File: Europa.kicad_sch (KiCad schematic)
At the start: 0 parts

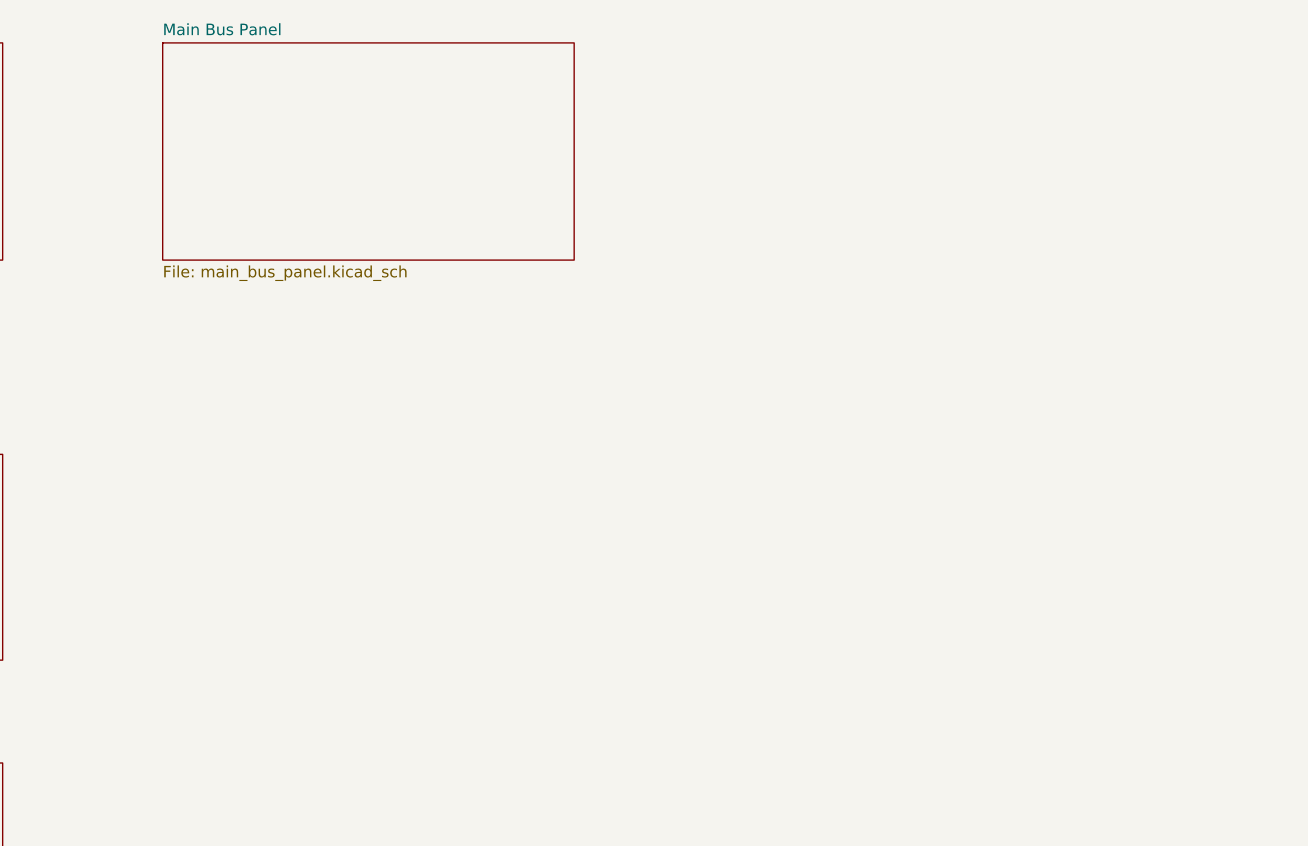
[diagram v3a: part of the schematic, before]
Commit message: Added Trim Circuit and Avionics Bus
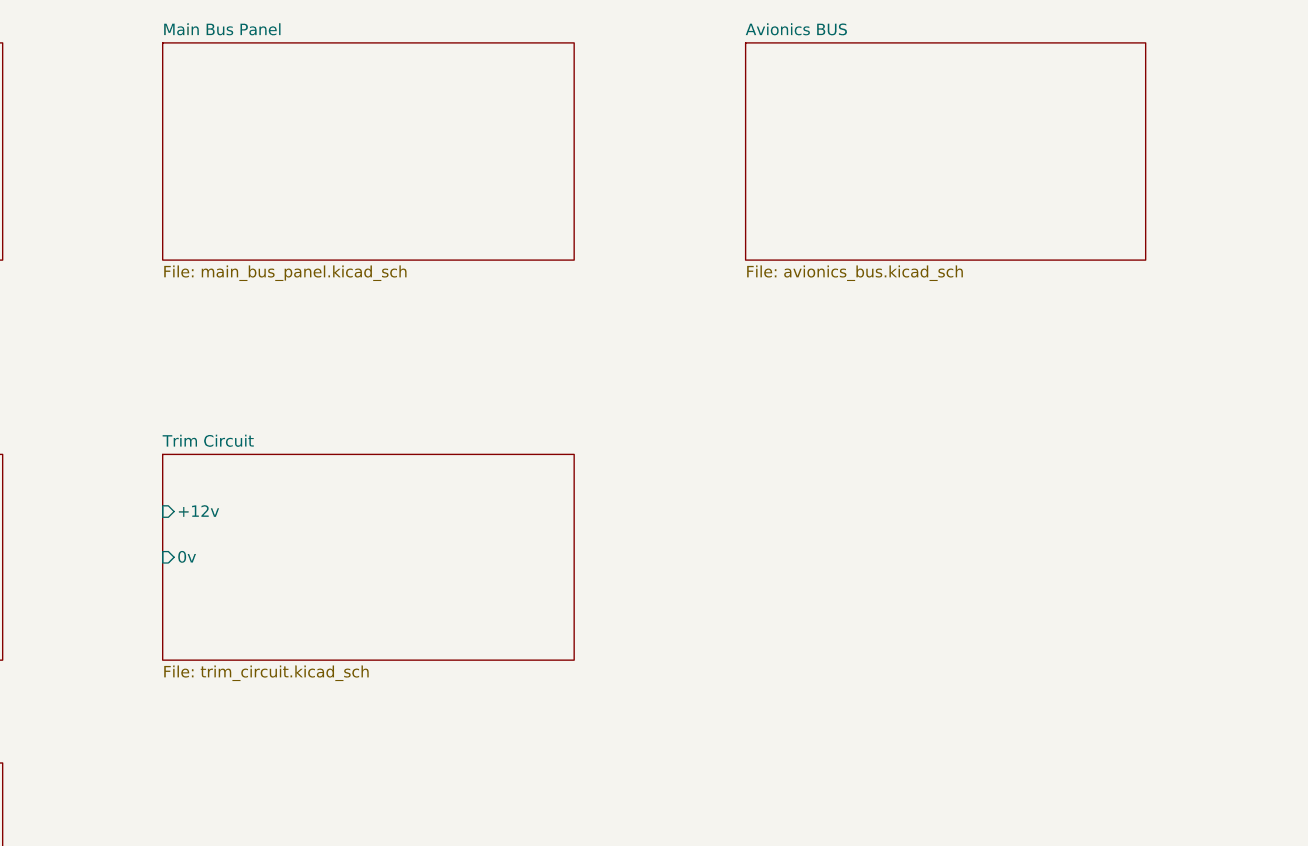
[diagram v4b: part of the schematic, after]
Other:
- added sheet Avionics BUS (avionics_bus.kicad_sch)
- added sheet Trim Circuit (trim_circuit.kicad_sch)
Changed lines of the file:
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@@
+    )
+  )
+  (sheet (at 157.48 29.21) (size 44.45 24.13) (fields_autoplaced)
+    (stroke (width 0.1524) (type solid) (color 0 0 0 0))
+    (fill (color 0 0 0 0.0000))
+    (property "Sheet name" "Avionics BUS" (id 0) (at 157.48 28.4984 0)
+      (effects (font (size 1.27 1.27)) (justify left bottom))
+    )
+    (property "Sheet file" "avionics_bus.kicad_sch" (id 1) (at 157.48 53.9246 0)
+      (effects (font (size 1.27 1.27)) (justify left top))
     )
   )
@@
     (property "Sheet file" "com.kicad_sch" (id 1) (at 232.41 114.8846 0)
       (effects (font (size 1.27 1.27)) (justify left top))
+    )
+  )
+  (sheet (at 92.71 74.93) (size 45.72 22.86) (fields_autoplaced)
+    (stroke (width 0.1524) (type solid) (color 0 0 0 0))
+    (fill (color 0 0 0 0.0000))
+    (property "Sheet name" "Trim Circuit" (id 0) (at 92.71 74.2184 0)
+      (effects (font (size 1.27 1.27)) (justify left bottom))
+    )
+    (property "Sheet file" "trim_circuit.kicad_sch" (id 1) (at 92.71 98.3746 0)
+      (effects (font (size 1.27 1.27)) (justify left top))
+    )
+    (pin "+12v" input (at 92.71 81.28 180)
+      (effects (font (size 1.27 1.27)) (justify left))
+    )
+    (pin "0v" input (at 92.71 86.36 180)
+      (effects (font (size 1.27 1.27)) (justify left))
     )
   )
@@
     (path "/c5676131-d5a4-4fde-914f-3f396c9cd255" (page "6"))
     (path "/e876c59e-4288-4b76-b538-81605be93f21" (page "7"))
+    (path "/866b3cfa-81f9-4c05-8259-46d4a400c4a9" (page "8"))
+    (path "/5afc04a8-14bc-4c25-8a7e-c4e01fd6c06c" (page "9"))
   )
   (symbol_instances
@@
       (reference "#PWR?") (unit 1) (value "GND") (footprint "")
     )
+    (path "/866b3cfa-81f9-4c05-8259-46d4a400c4a9/d0c3bae4-0af2-4e00-b106-8d7e92467906"
+      (reference "#PWR?") (unit 1) (value "GND") (footprint "")
+    )
     (path "/95e96eec-8054-412c-b439-e274da9864da/d8bf2695-17a9-416c-aba7-6777ceba8849"
+      (reference "#PWR?") (unit 1) (value "GND") (footprint "")
+    )
+    (path "/e876c59e-4288-4b76-b538-81605be93f21/e3dea152-b7e9-4b86-892e-d6d245a5440c"
+      (reference "#PWR?") (unit 1) (value "GND") (footprint "")
+    )
+    (path "/866b3cfa-81f9-4c05-8259-46d4a400c4a9/f5636c71-23a5-4c88-8117-e2a6e826ce57"
       (reference "#PWR?") (unit 1) (value "GND") (footprint "")
     )
@@
       (reference "CB?") (unit 1) (value "RDAC CB") (footprint "")
     )
+    (path "/5afc04a8-14bc-4c25-8a7e-c4e01fd6c06c/369404a4-9680-4315-bc28-57fc9db44996"
+      (reference "CB?") (unit 1) (value "Avionics Bus CB") (footprint "")
+    )
     (path "/e876c59e-4288-4b76-b538-81605be93f21/388762f5-890b-46d3-9653-5b33ed052fa1"
       (reference "CB?") (unit 1) (value "Battery Master CB") (footprint "")
@@
       (reference "CB?") (unit 1) (value "Lamps CB") (footprint "")
     )
+    (path "/866b3cfa-81f9-4c05-8259-46d4a400c4a9/8c04583f-084d-417b-adcb-af5504f6662f"
+      (reference "CB?") (unit 1) (value "CircuitBreaker_1P") (footprint "")
+    )
     (path "/e876c59e-4288-4b76-b538-81605be93f21/91d337f0-0505-4fcb-92a1-e365f6ea2f61"
       (reference "CB?") (unit 1) (value "TRIM CB") (footprint "")
@@
       (reference "J4") (unit 1) (value "Screw_Terminal_01x12") (footprint "")
     )
+    (path "/866b3cfa-81f9-4c05-8259-46d4a400c4a9/1fb7f398-44df-4201-bc2f-b642988d115e"
+      (reference "J?") (unit 1) (value "PL?") (footprint "")
+    )
     (path "/c5676131-d5a4-4fde-914f-3f396c9cd255/2b931534-dcf4-4f0a-91cc-dc769096fa05"
       (reference "J?") (unit 1) (value "DB9_Female") (footprint "")
@@
       (reference "J?") (unit 1) (value "DB15_Male") (footprint "")
     )
+    (path "/866b3cfa-81f9-4c05-8259-46d4a400c4a9/3fd3a499-d077-4b88-94d8-a82d86dba2b8"
+      (reference "J?") (unit 1) (value "PL?") (footprint "")
+    )
     (path "/e876c59e-4288-4b76-b538-81605be93f21/619ed128-9b69-4240-9409-37a06185dd84"
       (reference "J?") (unit 1) (value "PL? - Fuel Pump") (footprint "")
@@
       (reference "J?") (unit 1) (value "DB25_Female") (footprint "")
     )
+    (path "/866b3cfa-81f9-4c05-8259-46d4a400c4a9/9c4ce566-e3f9-4617-a008-e8f5eae99ff8"
+      (reference "J?") (unit 1) (value "PL15/3") (footprint "")
+    )
     (path "/c5676131-d5a4-4fde-914f-3f396c9cd255/9d2c5c72-5033-4e18-8ccb-6942d4705a16"
       (reference "J?") (unit 1) (value "DB15_Female") (footprint "")
@@
       (reference "J?") (unit 1) (value "DB15_Male") (footprint "")
     )
+    (path "/5afc04a8-14bc-4c25-8a7e-c4e01fd6c06c/b68e1cf4-a1ec-46c0-9ae1-d5bf2316ba50"
+      (reference "J?") (unit 1) (value "ECB Outputs") (footprint "")
+    )
     (path "/c5676131-d5a4-4fde-914f-3f396c9cd255/c04e6087-e529-408a-8a03-5605e6e4e80a"
       (reference "J?") (unit 1) (value "DB15_Female") (footprint "")
@@
       (reference "J?") (unit 1) (value "DB9_Male") (footprint "")
     )
+    (path "/866b3cfa-81f9-4c05-8259-46d4a400c4a9/cc93d801-b764-4613-8402-e8ad74cecd74"
+      (reference "J?") (unit 1) (value "PL?") (footprint "")
+    )
     (path "/c5676131-d5a4-4fde-914f-3f396c9cd255/d008d60e-b61b-4155-beb9-5029ffe66249"
       (reference "J?") (unit 1) (value "DB9_Male") (footprint "")
     )
+    (path "/866b3cfa-81f9-4c05-8259-46d4a400c4a9/d80e3ef4-71ab-401a-85af-2c0cbb43f9c9"
+      (reference "J?") (unit 1) (value "PL?") (footprint "")
+    )
+    (path "/5afc04a8-14bc-4c25-8a7e-c4e01fd6c06c/dd7940dc-a753-4039-9d10-ba42224e15f4"
+      (reference "J?") (unit 1) (value "DB9_Female") (footprint "")
+    )
     (path "/a5352cd5-5c6a-411a-b1fe-0b8c42ec40dc/e77952fd-3f26-43bd-9da9-266d1d56298c"
       (reference "J?") (unit 1) (value "DB9_Female") (footprint "")
     )
+    (path "/5afc04a8-14bc-4c25-8a7e-c4e01fd6c06c/f42ae037-2e0e-42dc-a666-25d17c484087"
+      (reference "J?") (unit 1) (value "Screw_Terminal_01x01") (footprint "")
+    )
+    (path "/5afc04a8-14bc-4c25-8a7e-c4e01fd6c06c/f8ad658e-16f3-423c-8f3d-ad5f4ce096af"
+      (reference "J?") (unit 1) (value "DB9_Male") (footprint "")
+    )
+    (path "/5afc04a8-14bc-4c25-8a7e-c4e01fd6c06c/fa3f87b1-63e0-4bcf-bfa3-d9d58049cb4a"
+      (reference "J?") (unit 1) (value "Conn_02x08_Odd_Even") (footprint "")
+    )
+    (path "/5afc04a8-14bc-4c25-8a7e-c4e01fd6c06c/fc3384d7-5dd0-4e7d-a6cd-f7d07b72acd5"
+      (reference "J?") (unit 1) (value "Conn_02x08_Odd_Even") (footprint "")
+    )
     (path "/95e96eec-8054-412c-b439-e274da9864da/381197e2-b232-4b8f-b646-39112473a836"
       (reference "LA?") (unit 1) (value "Alternator Warning Lamp") (footprint "")
     )
-    (path "/e876c59e-4288-4b76-b538-81605be93f21/5bf7dce5-2000-421b-958d-68d2519ed3ba"
-      (reference "LA?") (unit 1) (value "Lamp") (footprint "")
-    )
-    (path "/e876c59e-4288-4b76-b538-81605be93f21/b6037f4d-1b39-4027-b890-d8a4414367a5"
-      (reference "LA?") (unit 1) (value "Lamp") (footprint "")
-    )
-    (path "/e876c59e-4288-4b76-b538-81605be93f21/da0418c1-ec5c-46e4-a289-eb3cf882a2aa"
-      (reference "LA?") (unit 1) (value "Lamp") (footprint "")
-    )
-    (path "/e876c59e-4288-4b76-b538-81605be93f21/e877879b-73eb-4bb6-a08d-a6923f98ec97"
-      (reference "LA?") (unit 1) (value "Lamp") (footprint "")
-    )
     (path "/c5676131-d5a4-4fde-914f-3f396c9cd255/8b3089c2-4205-4106-b1c3-6349d2fe7f00"
       (reference "Lamps-CB") (unit 1) (value "CircuitBreaker_1P") (footprint "")
@@
       (reference "PL?") (unit 1) (value "PL9/7") (footprint "")
     )
+    (path "/5afc04a8-14bc-4c25-8a7e-c4e01fd6c06c/b42ac1f6-59d0-4f2c-85ba-9a1f496fb2b0"
+      (reference "PL?") (unit 1) (value "Conn_01x02_Female") (footprint "")
+    )
+    (path "/5afc04a8-14bc-4c25-8a7e-c4e01fd6c06c/df97c55f-1341-4a8a-b2cf-047088d5ab54"
+      (reference "PL?") (unit 1) (value "Conn_01x02_Male") (footprint "")
+    )
     (path "/e876c59e-4288-4b76-b538-81605be93f21/f8d87646-0d96-4cd5-a3d1-535558283599"
       (reference "PL?") (unit 1) (value "PL15/2") (footprint "")
@@
       (reference "SW?") (unit 1) (value "Starter Switch") (footprint "")
     )
+    (path "/866b3cfa-81f9-4c05-8259-46d4a400c4a9/60c35ef3-d4a2-422d-8aa1-05015c9cc7bb"
+      (reference "SW?") (unit 1) (value "SW_SPDT_MSM") (footprint "")
+    )
     (path "/e876c59e-4288-4b76-b538-81605be93f21/afecc038-43b6-458e-aa63-20b51e6acf0e"
       (reference "SW?") (unit 1) (value "Battery Master Switch") (footprint "")
     )
+    (path "/866b3cfa-81f9-4c05-8259-46d4a400c4a9/caedda76-3cac-49ed-a9bc-0931ab29328c"
+      (reference "SW?") (unit 1) (value "SW_SPDT_MSM") (footprint "")
+    )
     (path "/e876c59e-4288-4b76-b538-81605be93f21/d4d62dba-6fe8-4f5c-afde-76945c0db595"
       (reference "SW?") (unit 1) (value "Starter Sw") (footprint "")
     )
+    (path "/5afc04a8-14bc-4c25-8a7e-c4e01fd6c06c/dba945de-b8cb-4087-86b9-ff9cb25ac9e6"
+      (reference "SW?") (unit 1) (value "Avionics Master") (footprint "")
+    )
     (path "/c5676131-d5a4-4fde-914f-3f396c9cd255/dbb84075-4131-47a3-b3a9-3ffe8d76ec2d"
       (reference "Starter-CB") (unit 1) (value "CircuitBreaker_1P") (footprint "")
@@
       (reference "U?") (unit 1) (value "OAT_Sensor") (footprint "")
     )
+    (path "/866b3cfa-81f9-4c05-8259-46d4a400c4a9/874f090a-da72-4fd3-8793-c404e1c00bfc"
+      (reference "U?") (unit 1) (value "Pitch_Trim_Servo") (footprint "")
+    )
+    (path "/866b3cfa-81f9-4c05-8259-46d4a400c4a9/c9f7875d-5829-42f5-94cf-ee5d8901ec4d"
+      (reference "U?") (unit 1) (value "Pitch_Trim_Indicator") (footprint "")
+    )
     (path "/95e96eec-8054-412c-b439-e274da9864da/e9eef6b0-61c9-45dc-a99e-e0a5e09e5289"

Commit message: Added Tag Blocks
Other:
- sheet COM renamed COM Radio
- added sheet SmartASS (smartass.kicad_sch)
- added sheet Tag Blocks (tagblocks.kicad_sch)
- sheet Transponder ports: added +12v, 0volt; removed none
- title: (none) -> Europa Electrical Wiring

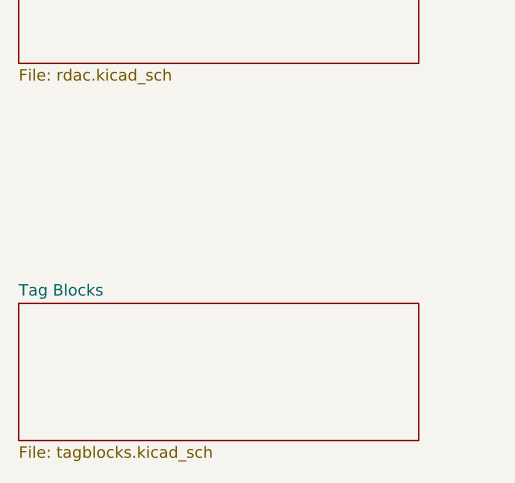
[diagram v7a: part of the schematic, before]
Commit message: Updates from manual validation
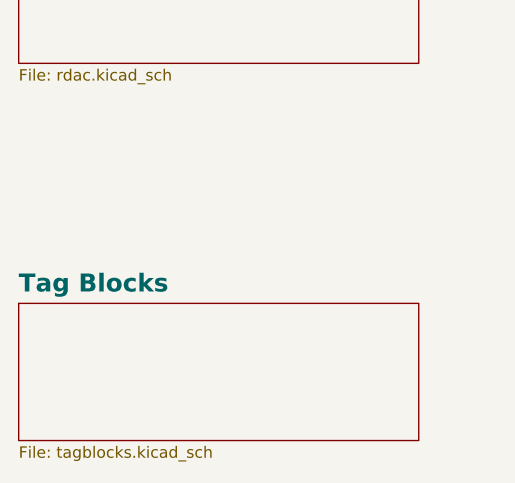
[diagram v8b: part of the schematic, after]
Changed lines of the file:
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@@
     (stroke (width 0.1524) (type solid) (color 0 0 0 0))
     (fill (color 0 0 0 0.0000))
-    (property "Sheet name" "Tag Blocks" (id 0) (at 29.21 155.4984 0)
-      (effects (font (size 1.27 1.27)) (justify left bottom))
+    (property "Sheet name" "Tag Blocks" (id 0) (at 29.21 155.1334 0)
+      (effects (font (size 2 2) bold) (justify left bottom))
     )
     (property "Sheet file" "tagblocks.kicad_sch" (id 1) (at 29.21 172.0346 0)
@@
       (reference "FB1/2") (unit 1) (value "Fuse") (footprint "")
     )
+    (path "/c5676131-d5a4-4fde-914f-3f396c9cd255/d485d247-bb20-4ffc-b2f5-e1c0eaafda4a"
+      (reference "FB1/2") (unit 1) (value "Fuse") (footprint "")
+    )
     (path "/e876c59e-4288-4b76-b538-81605be93f21/5ace1d45-19fe-4a6c-a4e1-f3444181a0f2"
       (reference "FB2/1") (unit 1) (value "Fuse") (footprint "")
@@
       (reference "FB2/4") (unit 1) (value "Fuse") (footprint "")
     )
-    (path "/c5676131-d5a4-4fde-914f-3f396c9cd255/d485d247-bb20-4ffc-b2f5-e1c0eaafda4a"
-      (reference "FS-2") (unit 1) (value "Fuse") (footprint "")
-    )
     (path "/293b5c94-66ed-4931-a87f-688673218b15/e89ba836-c472-4e6e-8283-7dec4cf43d20"
       (reference "J1") (unit 1) (value "Antenna SMA") (footprint "")
     )
-    (path "/293b5c94-66ed-4931-a87f-688673218b15/ebe3f642-9b43-430a-b037-7f70139ef68a"
-      (reference "J2") (unit 1) (value "DB15_Female") (footprint "")
-    )
     (path "/293b5c94-66ed-4931-a87f-688673218b15/acbdb600-6467-47ff-9f07-fa11e9815756"
       (reference "J3") (unit 1) (value "Screw_Terminal_01x08") (footprint "")
@@
       (reference "J?") (unit 1) (value "PL5-B") (footprint "")
     )
-    (path "/c5676131-d5a4-4fde-914f-3f396c9cd255/2b931534-dcf4-4f0a-91cc-dc769096fa05"
-      (reference "J?") (unit 1) (value "DB9_Female") (footprint "")
-    )
     (path "/c5676131-d5a4-4fde-914f-3f396c9cd255/2eedac69-ebdc-4a09-ab2c-65c33d3be8e3"
       (reference "J?") (unit 1) (value "DB15_Male") (footprint "")
@@
       (reference "J?") (unit 1) (value "PL4-A") (footprint "")
     )
-    (path "/c5676131-d5a4-4fde-914f-3f396c9cd255/d008d60e-b61b-4155-beb9-5029ffe66249"
-      (reference "J?") (unit 1) (value "DB9_Male") (footprint "")
-    )
     (path "/866b3cfa-81f9-4c05-8259-46d4a400c4a9/d80e3ef4-71ab-401a-85af-2c0cbb43f9c9"
       (reference "J?") (unit 1) (value "PL4-B") (footprint "")
@@
       (reference "PL1-B") (unit 1) (value "Conn_01x02_Male") (footprint "")
     )
+    (path "/e876c59e-4288-4b76-b538-81605be93f21/99240c25-009b-4d05-8923-121bbd3fbb5d"
+      (reference "PL1A") (unit 1) (value "Conn_01x03_Female") (footprint "")
+    )
     (path "/5afc04a8-14bc-4c25-8a7e-c4e01fd6c06c/b42ac1f6-59d0-4f2c-85ba-9a1f496fb2b0"
       (reference "PL2") (unit 1) (value "Conn_01x02_Female") (footprint "")
@@
       (reference "PL2") (unit 1) (value "Conn_01x02_Male") (footprint "")
     )
+    (path "/c5676131-d5a4-4fde-914f-3f396c9cd255/d008d60e-b61b-4155-beb9-5029ffe66249"
+      (reference "PL3A") (unit 1) (value "DB9_Male") (footprint "")
+    )
+    (path "/c5676131-d5a4-4fde-914f-3f396c9cd255/2b931534-dcf4-4f0a-91cc-dc769096fa05"
+      (reference "PL3B") (unit 1) (value "DB9_Female") (footprint "")
+    )
     (path "/c5676131-d5a4-4fde-914f-3f396c9cd255/559ccf97-058c-431a-aa6c-8b448def102e"
       (reference "PL9-A") (unit 1) (value "DB15_Female") (footprint "")
@@
     )
     (path "/95e96eec-8054-412c-b439-e274da9864da/6549f19e-d7ae-423b-90b3-e880a9f61d6c"
-      (reference "PL9/2") (unit 1) (value "Conn_01x01") (footprint "")
-    )
-    (path "/a5352cd5-5c6a-411a-b1fe-0b8c42ec40dc/c010279e-e885-425a-8dde-29e99d1e0e11"
-      (reference "PL10-F") (unit 1) (value "Conn_01x03_Female") (footprint "")
-    )
-    (path "/a5352cd5-5c6a-411a-b1fe-0b8c42ec40dc/94b0ac53-6566-4d3b-8667-5342e6dfb189"
-      (reference "PL10-M") (unit 1) (value "Conn_01x03_Male") (footprint "")
+      (reference "PL9/9") (unit 1) (value "Conn_01x01") (footprint "")
     )
     (path "/a5352cd5-5c6a-411a-b1fe-0b8c42ec40dc/2409a3e3-f0dc-4e5d-8d6e-71c8c1c58eb7"
       (reference "PL12/1") (unit 1) (value "Conn_01x01") (footprint "")
     )
+    (path "/e876c59e-4288-4b76-b538-81605be93f21/8d8510c9-92e8-47fc-ab6d-ff99756c29f2"
+      (reference "PL12B") (unit 1) (value "Conn_01x03_Male") (footprint "")
+    )
     (path "/a5352cd5-5c6a-411a-b1fe-0b8c42ec40dc/32b7ec03-c573-4fc2-9f00-e104d3f42467"
       (reference "PL15") (unit 1) (value "Conn_01x03_Male") (footprint "")
@@
       (reference "PL15/1") (unit 1) (value "Conn_01x01") (footprint "")
     )
+    (path "/c5676131-d5a4-4fde-914f-3f396c9cd255/3dbb45a6-75bf-4d19-9846-bff05e48f5f7"
+      (reference "PL15/2") (unit 1) (value "Conn_01x01") (footprint "")
+    )
     (path "/95e96eec-8054-412c-b439-e274da9864da/efba767d-032c-4fc0-ac0f-c7b5004e101c"
       (reference "PL15/2") (unit 1) (value "Conn_01x01") (footprint "")
@@
       (reference "PL15/3") (unit 1) (value "Conn_01x01") (footprint "")
     )
+    (path "/c5676131-d5a4-4fde-914f-3f396c9cd255/a32f2c43-e7f4-4eff-8fbf-9407f2509aae"
+      (reference "PL15/4") (unit 1) (value "Conn_01x01") (footprint "")
+    )
+    (path "/e876c59e-4288-4b76-b538-81605be93f21/d7eb02da-e535-40f9-b06b-cb6c3c8dd4be"
+      (reference "PL15/4") (unit 1) (value "PL9/14") (footprint "")
+    )
+    (path "/5afc04a8-14bc-4c25-8a7e-c4e01fd6c06c/44e5cdc4-7be7-470a-aadd-56aa1a6bb9c6"
+      (reference "PL15/6") (unit 1) (value "Conn_01x01") (footprint "")
+    )
     (path "/95e96eec-8054-412c-b439-e274da9864da/1c9a909b-961c-49c2-879c-f646c2a2f1a5"
       (reference "PL15/9") (unit 1) (value "Conn_01x01") (footprint "")
@@
       (reference "PL15/10") (unit 1) (value "Conn_01x01") (footprint "")
     )
+    (path "/293b5c94-66ed-4931-a87f-688673218b15/ebe3f642-9b43-430a-b037-7f70139ef68a"
+      (reference "PL16") (unit 1) (value "DB15_Female") (footprint "")
+    )
     (path "/e876c59e-4288-4b76-b538-81605be93f21/02428102-6ae6-4d41-9989-a38e205d44b5"
